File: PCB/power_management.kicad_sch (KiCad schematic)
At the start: 0 parts

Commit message: Polarity protection in Power Management
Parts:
- added D1: D, symbol Device:D
- added D2: 10V, symbol Device:D_Zener
- added J5: MainPower, Connector_Phoenix_MC:PhoenixContact_MCV_1,5_2-G-3.5_1x02_P3.50mm_Vertical, symbol Connector_Generic:Conn_01x02
- added J7, J8: Ignition 12V, Connector_Phoenix_MC:PhoenixContact_MCV_1,5_2-G-3.5_1x02_P3.50mm_Vertical, symbol Connector_Generic:Conn_01x02
- added Q1: PMOS, symbol Simulation_SPICE:PMOS
- added R1 (x2): 110k, Resistor_SMD:R_0603_1608Metric_Pad0.98x0.95mm_HandSolder, symbol Device:R
- added R1: 470k, Resistor_SMD:R_0603_1608Metric_Pad0.98x0.95mm_HandSolder, symbol Device:R
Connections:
- new net: D2.2 (A), Q1.2 (G), R1.2
- new net: D1.2 (A), J5.2 (Pin_2), Q1.1 (D)
- new net GND: J5.1 (Pin_1), R1.1, R1.1
- new net VCC_INPUT: D1.1 (K), D2.1 (K), Q1.3 (S), R1.2
- new net VCC_INPUT_A: R1.1, R1.2
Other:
- note added: "D1 is only an alternative to Q1"

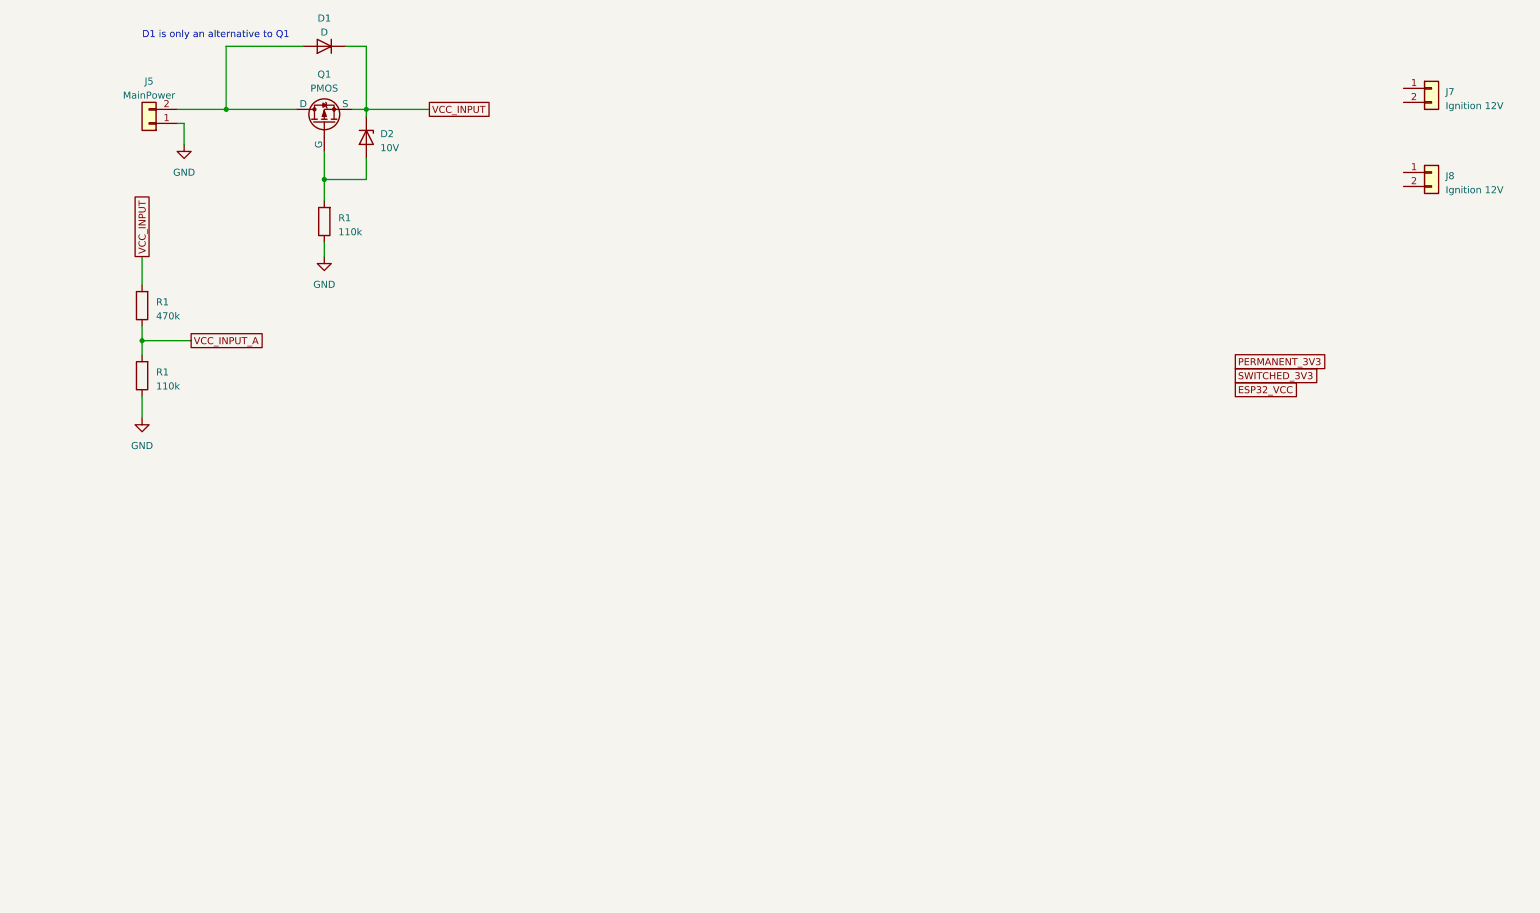
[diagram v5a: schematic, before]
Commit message: Input voltage protection added
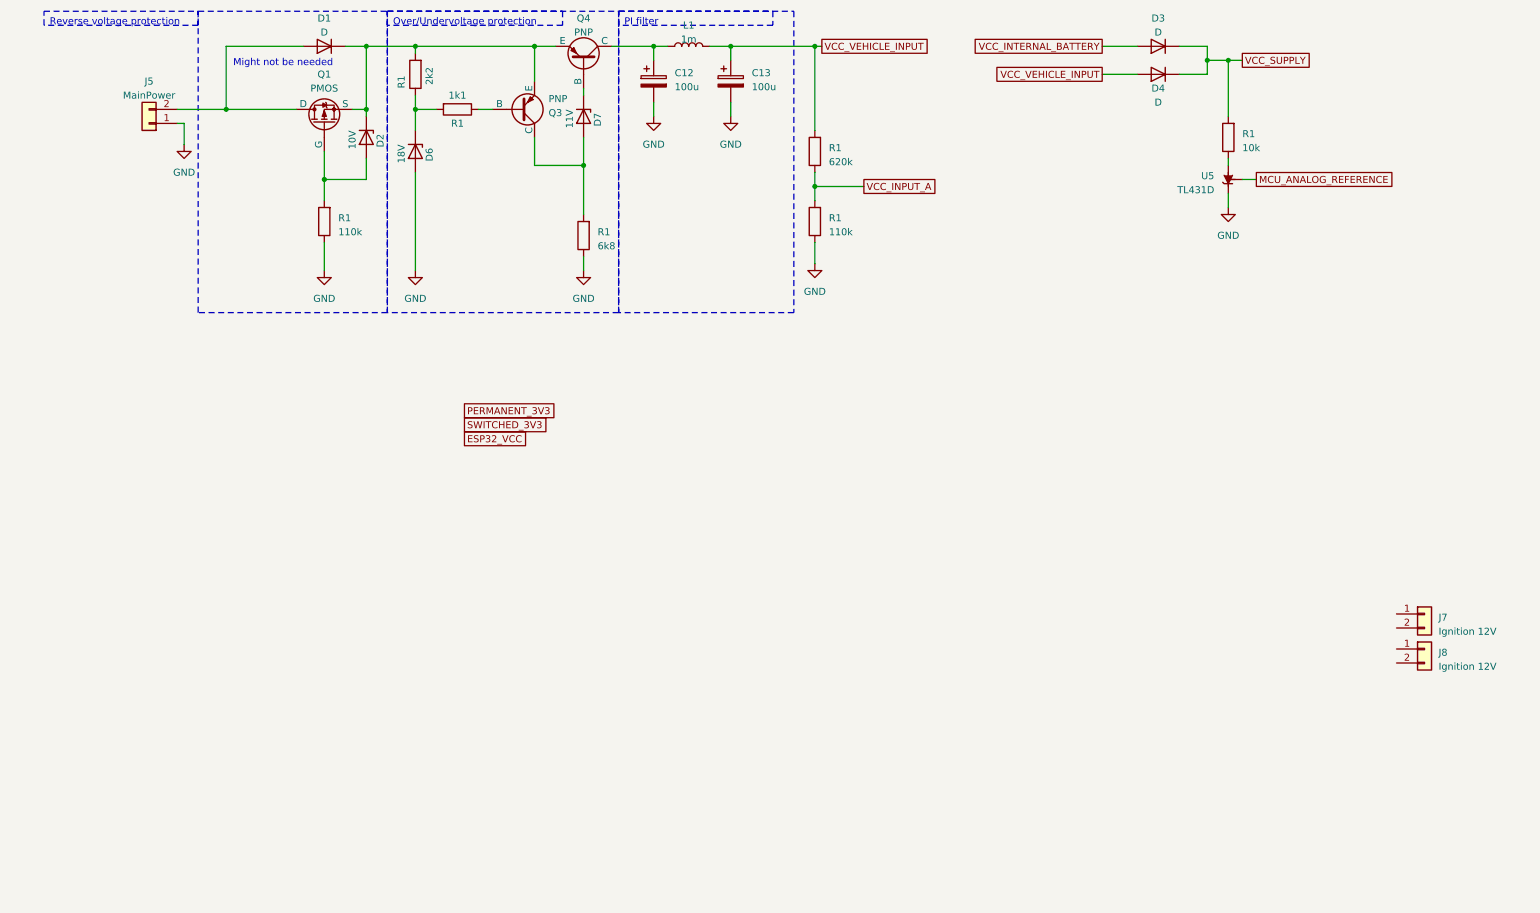
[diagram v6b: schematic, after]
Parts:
- added C12, C13: 100u, symbol Device:C_Polarized
- added D3, D4: D, symbol Device:D
- added D6: 18V, symbol Device:D_Zener
- added D7: 11V, symbol Device:D_Zener
- added L1: 1m, symbol Device:L
- added Q3, Q4: PNP, symbol Simulation_SPICE:PNP
- added R1: 6k8, Resistor_SMD:R_0603_1608Metric_Pad0.98x0.95mm_HandSolder, symbol Device:R
- added R1: 10k, Resistor_SMD:R_0603_1608Metric_Pad0.98x0.95mm_HandSolder, symbol Device:R
- added R1: 2k2, Resistor_SMD:R_0603_1608Metric_Pad0.98x0.95mm_HandSolder, symbol Device:R
- added R1: 1k1, Resistor_SMD:R_0603_1608Metric_Pad0.98x0.95mm_HandSolder, symbol Device:R
- added U5: TL431D, Package_SO:SOIC-8_3.9x4.9mm_P1.27mm, symbol Reference_Voltage:TL431D
- R1: value 470k -> 620k
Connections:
- net GND: now also C12.2, C13.2, D6.2 (A), R1.1, U5.1 (K)
- net VCC_INPUT: no longer names the net of D1.1 (K), D2.1 (K), Q1.3 (S)
- net VCC_INPUT: now also Q3.3 (E), Q4.3 (E), R1.2; no longer R1.2
- new net: D7.1 (K), Q4.2 (B)
- new net: D7.2 (A), Q3.1 (C), R1.2
- new net: R1.1, U5.2 (A), U5.3 (A), U5.6 (A), U5.7 (A)
- new net: Q3.2 (B), R1.1
- new net: D6.1 (K), R1.1, R1.2
- new net: C12.1, L1.1, Q4.1 (C)
- new net MCU_ANALOG_REFERENCE: U5.8 (REF)
- new net VCC_INTERNAL_BATTERY: D3.2 (A)
- new net VCC_SUPPLY: D3.1 (K), D4.1 (K), R1.2
- new net VCC_VEHICLE_INPUT: C13.1, D4.2 (A), L1.2, R1.2
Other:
- note added: "Might not be needed"
- note removed: "D1 is only an alternative to Q1"
- moved on the sheet: J7, J8, R1

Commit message: Added permanent PSU
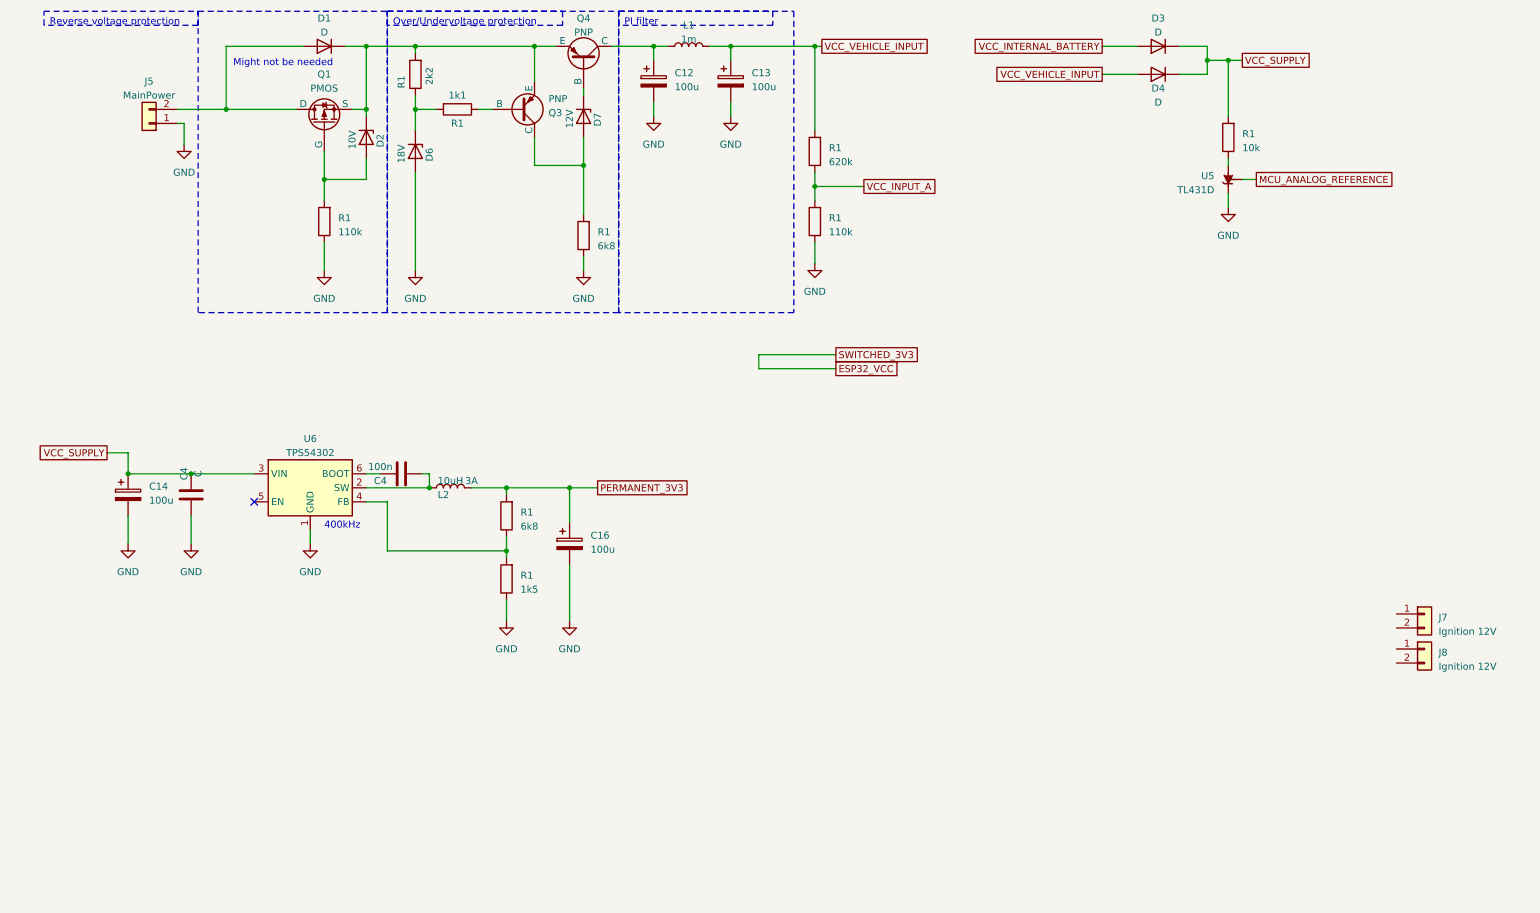
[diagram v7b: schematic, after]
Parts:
- added C14, C16: 100u, symbol Device:C_Polarized
- added C4: C, Capacitor_SMD:C_0201_0603Metric_Pad0.64x0.40mm_HandSolder, symbol Device:C
- added C4: 100n, Capacitor_SMD:C_0201_0603Metric_Pad0.64x0.40mm_HandSolder, symbol Device:C
- added L2: 10uH, symbol Device:L
- added R1: 6k8, Resistor_SMD:R_0603_1608Metric_Pad0.98x0.95mm_HandSolder, symbol Device:R
- added R1: 1k5, Resistor_SMD:R_0603_1608Metric_Pad0.98x0.95mm_HandSolder, symbol Device:R
- added U6: TPS54302, Package_TO_SOT_SMD:TO-263-4, symbol Regulator_Switching:TPS54302
- D7: value 11V -> 12V
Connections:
- net GND: now also C14.2, C16.2, C4.2, R1.1, U6.1 (GND)
- net PERMANENT_3V3: now also C16.1, L2.2, R1.2
- net VCC_SUPPLY: now also C14.1, C4.1, U6.3 (VIN)
- new net: R1.1, R1.2, U6.4 (FB)
- new net: C4.2, L2.1, U6.2 (SW)
- new net: C4.1, U6.6 (BOOT)
- no-connect marks 0 -> 1
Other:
- note added: "400kHz"

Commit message: A bit of advancement in power and battery management
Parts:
- added C18, C21: 100u, symbol Device:C_Polarized
- added C4: 100n, Capacitor_SMD:C_0201_0603Metric_Pad0.64x0.40mm_HandSolder, symbol Device:C
- added C4: C, Capacitor_SMD:C_0201_0603Metric_Pad0.64x0.40mm_HandSolder, symbol Device:C
- added L3: 10uH, symbol Device:L
- added R1: 1k5, Resistor_SMD:R_0603_1608Metric_Pad0.98x0.95mm_HandSolder, symbol Device:R
- added R1: 6k8, Resistor_SMD:R_0603_1608Metric_Pad0.98x0.95mm_HandSolder, symbol Device:R
- added U7: TPS54302, Package_TO_SOT_SMD:TO-263-4, symbol Regulator_Switching:TPS54302
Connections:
- net ESP32_VCC: now also C21.1, L3.2, R1.2
- net GND: now also C18.2, C21.2, C4.2, R1.1, U7.1 (GND)
- net VCC_SUPPLY: now also C18.1, C4.1, U7.3 (VIN)
- new net: R1.1, R1.2, U7.4 (FB)
- new net: C4.2, L3.1, U7.2 (SW)
- new net: C4.1, U7.6 (BOOT)
- new net ENABLE_SECONDARY_PSU: U7.5 (EN)
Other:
- moved on the sheet: J7, J8
